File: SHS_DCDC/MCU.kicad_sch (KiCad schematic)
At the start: 13 parts, among them J3 Conn_ARM_JTAG_SWD_10, U6 ESP32-S2-MINI-1, U8 MIC5501-3.0YM5, Y1 2-SMD no lead

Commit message: PV & BAT V sense
Adding 2 same blocks allowing the measure by ADC of the PV and Battery voltage on demand through power gating technique
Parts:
- added J4: Conn_01x02_Male, Connector_PinHeader_2.54mm:PinHeader_1x02_P2.54mm_Vertical, symbol Connector:Conn_01x02_Male
- added R28: 499, Resistor_SMD:R_0402_1005Metric, symbol Device:R
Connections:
- net MCU_RX: now also U6.40 (GPIO44/U0RXD/PROG), J4.1 (Pin_1)
- net MCU_TX: now also J4.2 (Pin_2), R28.1
- net at U6.39 (GPIO43/U0TXD/PROG): now also R28.2
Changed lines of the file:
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@@
   (junction (at 41.91 102.87) (diameter 0) (color 0 0 0 0)
   )
+  (junction (at 259.08 80.01) (diameter 0) (color 0 0 0 0)
+  )
   (junction (at 194.31 31.75) (diameter 0) (color 0 0 0 0)
   )
@@
   (junction (at 99.06 87.63) (diameter 0) (color 0 0 0 0)
   )
+  (junction (at 256.54 82.55) (diameter 0) (color 0 0 0 0)
+  )
   (junction (at 66.04 143.51) (diameter 0) (color 0 0 0 0)
   )
@@
     (stroke (width 0) (type default) (color 0 0 0 0))
   )
+  (wire (pts (xy 259.08 80.01) (xy 259.08 66.04))
+    (stroke (width 0) (type default) (color 0 0 0 0))
+  )
   (wire (pts (xy 96.52 80.01) (xy 99.06 80.01))
     (stroke (width 0) (type default) (color 0 0 0 0))
   )
+  (wire (pts (xy 256.54 82.55) (xy 256.54 63.5))
+    (stroke (width 0) (type default) (color 0 0 0 0))
+  )
   (wire (pts (xy -41.91 119.38) (xy -22.86 119.38))
     (stroke (width 0) (type default) (color 0 0 0 0))
   )
+  (wire (pts (xy 259.08 80.01) (xy 262.89 80.01))
+    (stroke (width 0) (type default) (color 0 0 0 0))
+  )
+  (wire (pts (xy 252.73 82.55) (xy 256.54 82.55))
+    (stroke (width 0) (type default) (color 0 0 0 0))
+  )
   (wire (pts (xy 66.04 139.7) (xy 66.04 143.51))
     (stroke (width 0) (type default) (color 0 0 0 0))
@@
     (stroke (width 0) (type default) (color 0 0 0 0))
   )
+  (wire (pts (xy 256.54 63.5) (xy 261.62 63.5))
+    (stroke (width 0) (type default) (color 0 0 0 0))
+  )
   (wire (pts (xy 118.11 130.81) (xy 118.11 127))
     (stroke (width 0) (type default) (color 0 0 0 0))
@@
     (stroke (width 0) (type default) (color 0 0 0 0))
   )
+  (wire (pts (xy 256.54 82.55) (xy 262.89 82.55))
+    (stroke (width 0) (type default) (color 0 0 0 0))
+  )
   (wire (pts (xy 143.51 143.51) (xy 66.04 143.51))
     (stroke (width 0) (type default) (color 0 0 0 0))
@@
     (stroke (width 0) (type default) (color 0 0 0 0))
   )
+  (wire (pts (xy 215.9 80.01) (xy 259.08 80.01))
+    (stroke (width 0) (type default) (color 0 0 0 0))
+  )
   (wire (pts (xy 92.71 160.02) (xy 143.51 160.02))
     (stroke (width 0) (type default) (color 0 0 0 0))
@@
     (stroke (width 0) (type default) (color 0 0 0 0))
   )
-  (wire (pts (xy -97.79 102.87) (xy -72.39 102.87))
-    (stroke (width 0) (type default) (color 0 0 0 0))
-  )
   (wire (pts (xy 207.01 26.67) (xy 214.63 26.67))
     (stroke (width 0) (type default) (color 0 0 0 0))
@@
     (stroke (width 0) (type default) (color 0 0 0 0))
   )
-  (wire (pts (xy -97.79 105.41) (xy -72.39 105.41))
-    (stroke (width 0) (type default) (color 0 0 0 0))
-  )
   (wire (pts (xy 215.9 135.89) (xy 227.33 135.89))
     (stroke (width 0) (type default) (color 0 0 0 0))
@@
     (stroke (width 0) (type default) (color 0 0 0 0))
   )
+  (wire (pts (xy 215.9 82.55) (xy 245.11 82.55))
+    (stroke (width 0) (type default) (color 0 0 0 0))
+  )
   (wire (pts (xy 99.06 80.01) (xy 99.06 87.63))
+    (stroke (width 0) (type default) (color 0 0 0 0))
+  )
+  (wire (pts (xy 259.08 66.04) (xy 261.62 66.04))
     (stroke (width 0) (type default) (color 0 0 0 0))
   )
@@
     )
   )
-  (global_label "MCU_RX" (shape input) (at -97.79 105.41 180) (fields_autoplaced)
-    (effects (font (size 1.27 1.27)) (justify right))
-    (property "Intersheet References" "${INTERSHEET_REFS}" (id 0) (at 0 0 0)
+  (global_label "MCU_RX" (shape input) (at 262.89 80.01 0) (fields_autoplaced)
+    (effects (font (size 1.27 1.27)) (justify left))
+    (property "Intersheet References" "${INTERSHEET_REFS}" (id 0) (at 165.1 185.42 0)
       (effects (font (size 1.27 1.27)) hide)
     )
@@
     )
   )
-  (global_label "MCU_TX" (shape input) (at -97.79 102.87 180) (fields_autoplaced)
-    (effects (font (size 1.27 1.27)) (justify right))
-    (property "Intersheet References" "${INTERSHEET_REFS}" (id 0) (at 0 0 0)
+  (global_label "MCU_TX" (shape input) (at 262.89 82.55 0) (fields_autoplaced)
+    (effects (font (size 1.27 1.27)) (justify left))
+    (property "Intersheet References" "${INTERSHEET_REFS}" (id 0) (at 165.1 185.42 0)
       (effects (font (size 1.27 1.27)) hide)
     )
@@
     (pin "1")
   )
+  (symbol (lib_id "Device:R") (at 248.92 82.55 270) (unit 1)
+    (in_bom yes) (on_board yes) (fields_autoplaced)
+    (property "Reference" "R28" (id 0) (at 248.92 76.2 90))
+    (property "Value" "499" (id 1) (at 248.92 78.74 90))
+    (property "Footprint" "Resistor_SMD:R_0402_1005Metric" (id 2) (at 248.92 80.772 90)
+      (effects (font (size 1.27 1.27)) hide)
+    )
+    (property "Datasheet" "~" (id 3) (at 248.92 82.55 0)
+      (effects (font (size 1.27 1.27)) hide)
+    )
+    (pin "1")
+    (pin "2")
+  )
   (symbol (lib_id "SHS_DCDC:GND-power") (at 246.38 62.23 0) (unit 1)
     (in_bom yes) (on_board yes)
@@
       (effects (font (size 1.27 1.27)) hide)
     )
+    (pin "1")
+    (pin "2")
+  )
+  (symbol (lib_id "Connector:Conn_01x02_Male") (at 266.7 66.04 180) (unit 1)
+    (in_bom yes) (on_board yes) (fields_autoplaced)
+    (property "Reference" "J4" (id 0) (at 267.97 63.4999 0)
+      (effects (font (size 1.27 1.27)) (justify right))
+    )
+    (property "Value" "Conn_01x02_Male" (id 1) (at 267.97 66.0399 0)
+      (effects (font (size 1.27 1.27)) (justify right))
+    )
+    (property "Footprint" "Connector_PinHeader_2.54mm:PinHeader_1x02_P2.54mm_Vertical" (id 2) (at 266.7 66.04 0)
+      (effects (font (size 1.27 1.27)) hide)
+    )
+    (property "Datasheet" "~" (id 3) (at 266.7 66.04 0)
+      (effects (font (size 1.27 1.27)) hide)
+    )

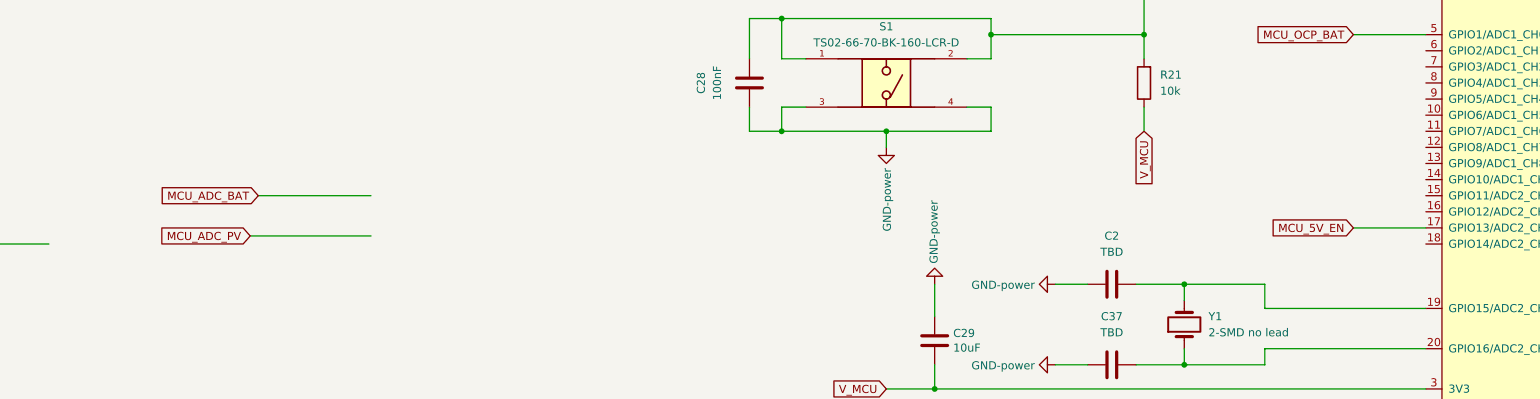
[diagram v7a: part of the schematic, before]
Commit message: ADC_PV & BAT
Blocks related to ADC reading of PV and BAT added on the physical board.
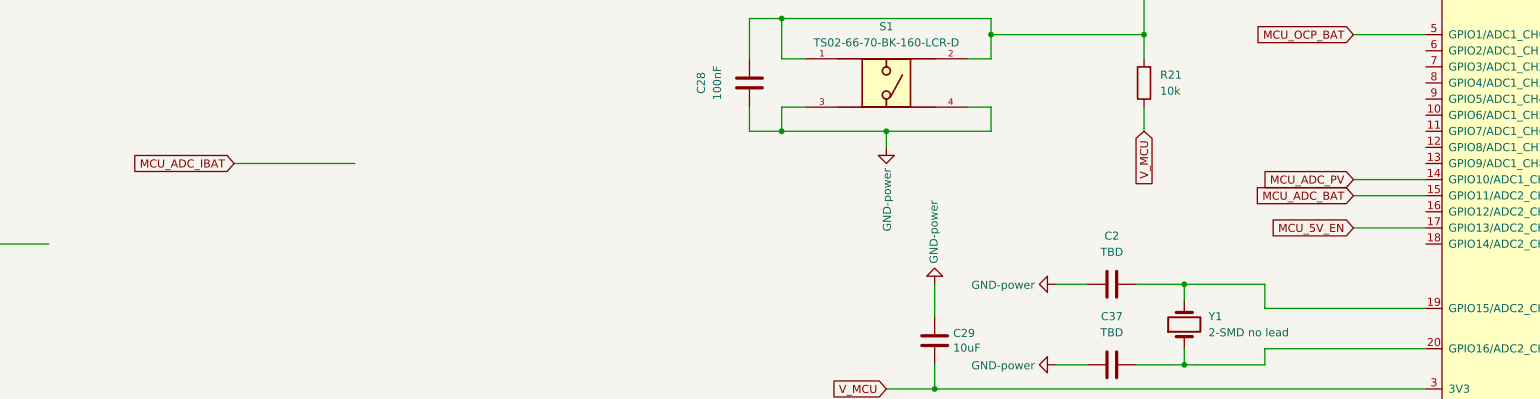
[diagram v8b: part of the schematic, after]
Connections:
- net MCU_ADC_BAT: now also U6.15 (GPIO11/ADC2_CH0)
- net MCU_ADC_PV: now also U6.14 (GPIO10/ADC1_CH9)
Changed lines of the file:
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@@
     (stroke (width 0) (type default) (color 0 0 0 0))
   )
-  (wire (pts (xy -41.91 119.38) (xy -22.86 119.38))
+  (wire (pts (xy 132.08 110.49) (xy 143.51 110.49))
     (stroke (width 0) (type default) (color 0 0 0 0))
   )
@@
     (stroke (width 0) (type default) (color 0 0 0 0))
   )
+  (wire (pts (xy -44.45 107.95) (xy -25.4 107.95))
+    (stroke (width 0) (type default) (color 0 0 0 0))
+  )
   (wire (pts (xy 36.83 85.09) (xy 41.91 85.09))
     (stroke (width 0) (type default) (color 0 0 0 0))
@@
     (stroke (width 0) (type default) (color 0 0 0 0))
   )
-  (wire (pts (xy -40.64 113.03) (xy -22.86 113.03))
+  (wire (pts (xy 132.08 113.03) (xy 143.51 113.03))
     (stroke (width 0) (type default) (color 0 0 0 0))
   )
@@
     )
   )
-  (global_label "MCU_ADC_BAT" (shape input) (at -40.64 113.03 180) (fields_autoplaced)
-    (effects (font (size 1.27 1.27)) (justify right))
-    (property "Intersheet References" "${INTERSHEET_REFS}" (id 0) (at 0 0 0)
-      (effects (font (size 1.27 1.27)) hide)
-    )
-  )
-  (global_label "MCU_ADC_PV" (shape input) (at -41.91 119.38 180) (fields_autoplaced)
-    (effects (font (size 1.27 1.27)) (justify right))
-    (property "Intersheet References" "${INTERSHEET_REFS}" (id 0) (at 0 0 0)
+  (global_label "MCU_ADC_BAT" (shape input) (at 132.08 113.03 180) (fields_autoplaced)
+    (effects (font (size 1.27 1.27)) (justify right))
+    (property "Intersheet References" "${INTERSHEET_REFS}" (id 0) (at 172.72 0 0)
+      (effects (font (size 1.27 1.27)) hide)
+    )
+  )
+  (global_label "MCU_ADC_PV" (shape input) (at 132.08 110.49 180) (fields_autoplaced)
+    (effects (font (size 1.27 1.27)) (justify right))
+    (property "Intersheet References" "${INTERSHEET_REFS}" (id 0) (at 173.99 -8.89 0)
       (effects (font (size 1.27 1.27)) hide)
     )
@@
     )
   )
+  (global_label "MCU_ADC_IBAT" (shape input) (at -44.45 107.95 180) (fields_autoplaced)
+    (effects (font (size 1.27 1.27)) (justify right))
+    (property "Intersheet References" "${INTERSHEET_REFS}" (id 0) (at -60.3209 107.8706 0)
+      (effects (font (size 1.27 1.27)) (justify right) hide)
+    )
+  )
